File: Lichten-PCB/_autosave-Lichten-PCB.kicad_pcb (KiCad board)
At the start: 2 copper layers, 54.2 x 62.2 mm, 56 parts, among them J1 Conn_01x04_Socket

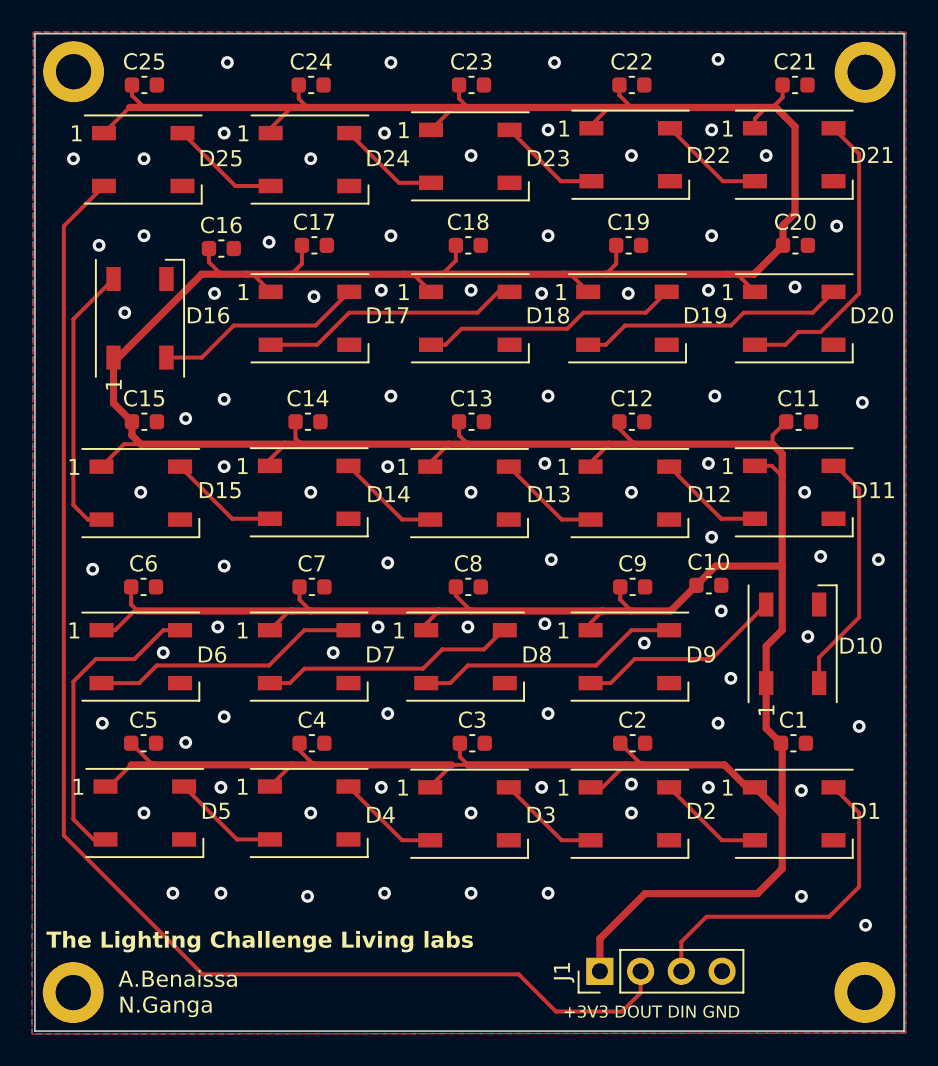
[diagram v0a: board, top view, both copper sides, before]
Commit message: Trace dikte en mounting hole toegevoegd
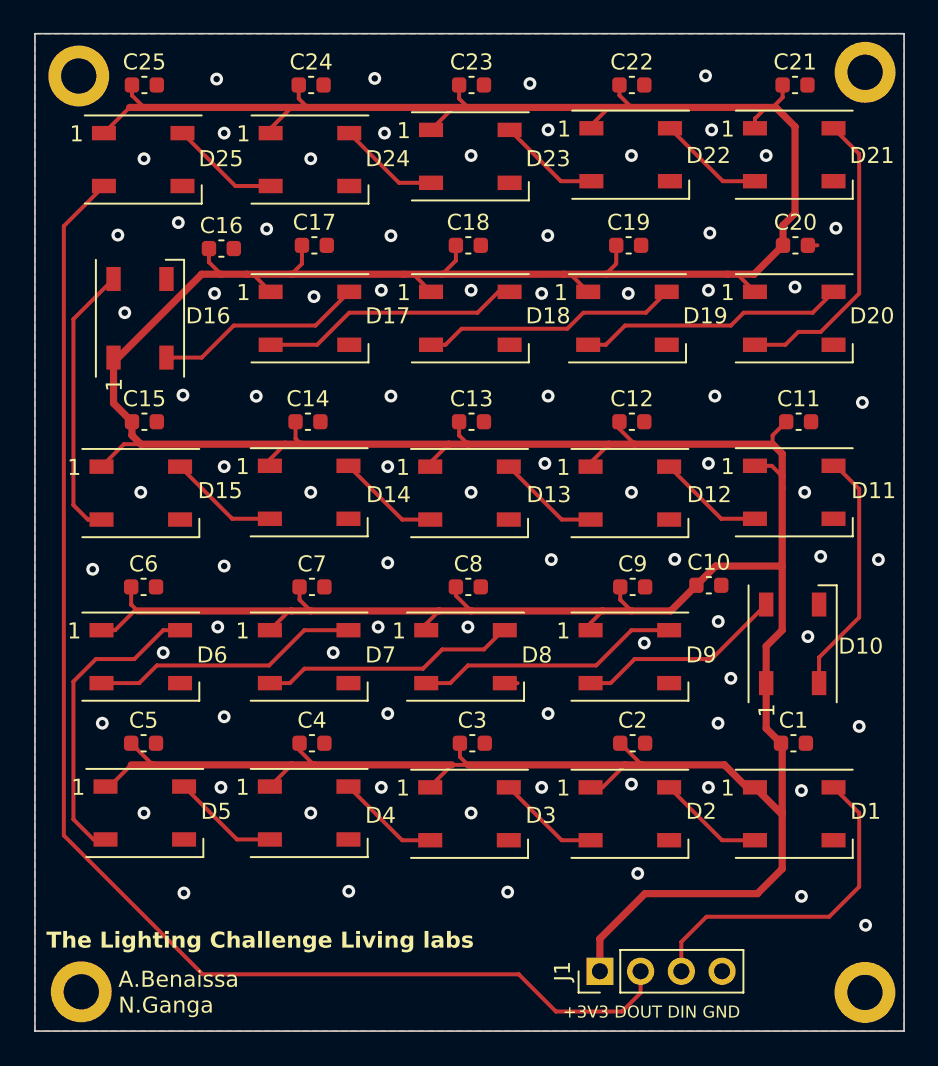
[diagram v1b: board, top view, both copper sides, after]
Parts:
- moved H3 0.50 mm to (121.1, 129.8)
- moved H2 0.42 mm to (120.9, 72.6)
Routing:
- net GND: track 0.00 -> 4.08 mm, vias 87 -> 81
